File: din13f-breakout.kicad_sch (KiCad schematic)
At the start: 5 parts, among them J1 DB15_Female_HighDensity, J2 RCJ-017, J3 Conn_01x13, J4 SDD-130J

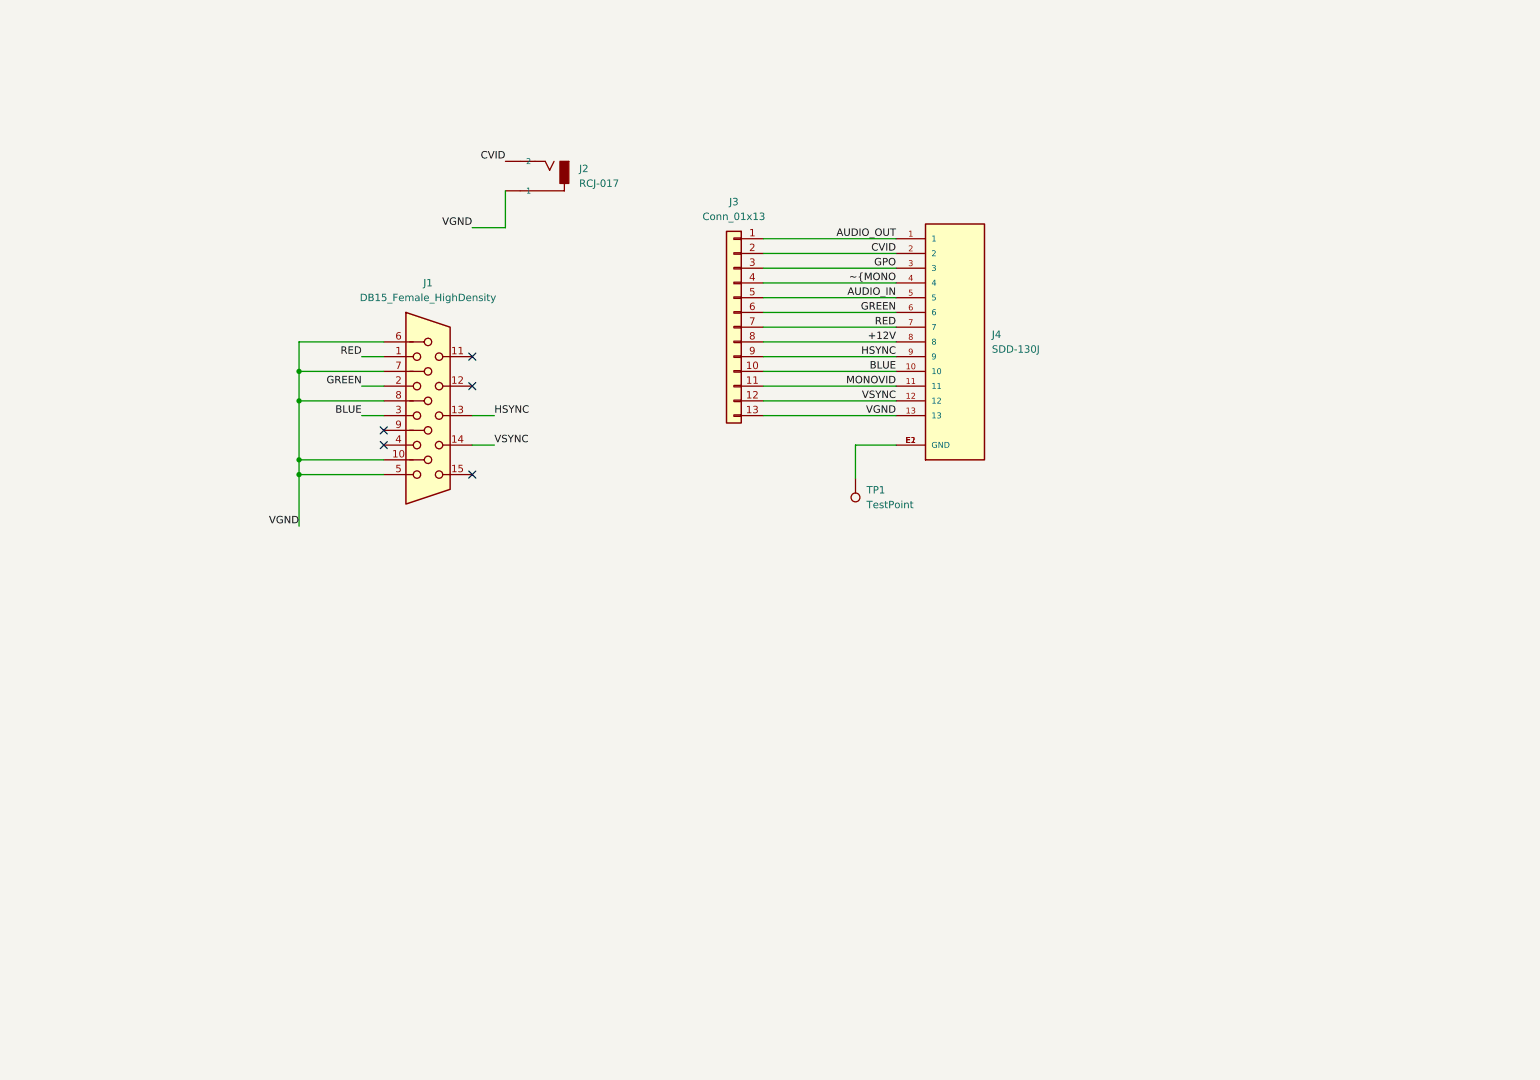
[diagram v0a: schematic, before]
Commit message: Draft of SCART version, no RGB voltage ampl yet
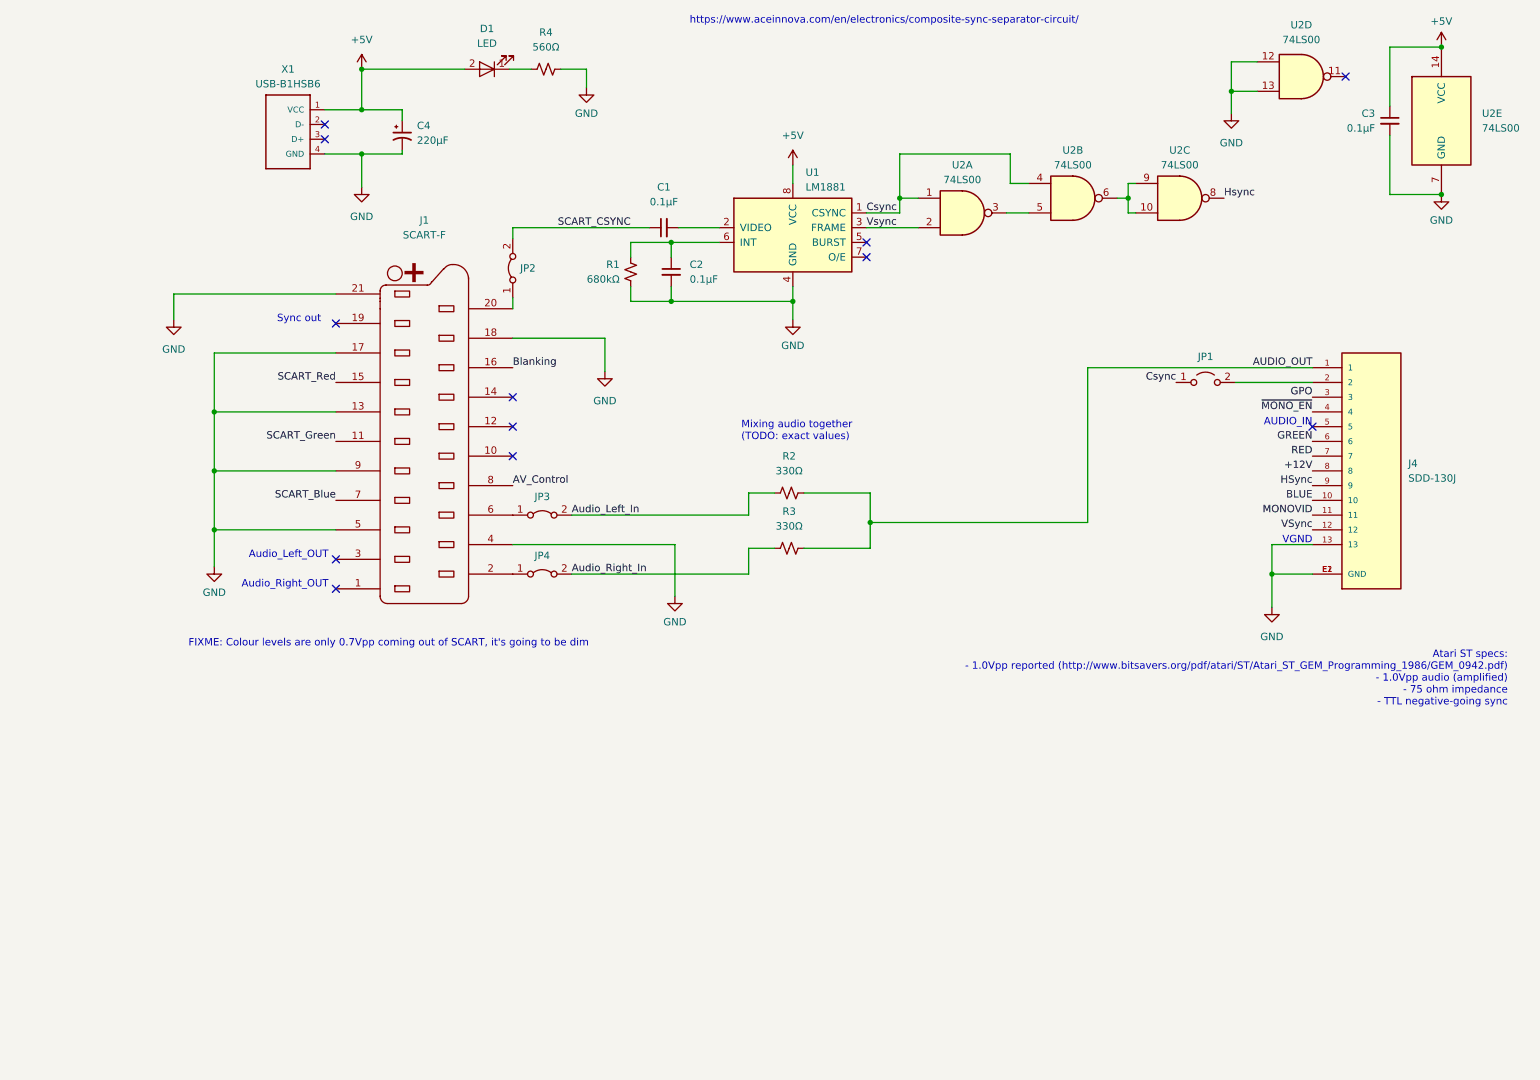
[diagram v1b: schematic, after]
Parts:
- removed J1: DB15_Female_HighDensity, Connector_TE_AMP_HD15:FIXED-1-1734530-1, symbol Connector:DB15_Female_HighDensity
- removed J2: RCJ-017, Jacks:CUI_RCJ-017, symbol RCJ-017:RCJ-017
- removed J3: Conn_01x13, Connectors:13p_GrabPads, symbol Connector_Generic:Conn_01x13
- removed TP1: TestPoint, TestPoint:TestPoint_Pad_2.5x2.5mm, symbol Connector:TestPoint
- added C1, C2, C3: 0.1µF, symbol Device:C_Small
- added C4: 220µF, symbol Device:C_Polarized_Small_US
- added D1: LED, LED_THT:LED_D3.0mm, symbol bkm-129x-scart-vga-rescue:LED
- added J1: SCART-F, ninigi-scart-ra:NINIGI-SCART-RA, symbol bkm-129x-scart-vga-rescue:SCART-F
- added JP1: Jumper_2_Open, Resistor_SMD:R_0805_2012Metric_Pad1.20x1.40mm_HandSolder, symbol Jumper:Jumper_2_Open
- added JP2, JP3, JP4: Jumper_2_Bridged, symbol Jumper:Jumper_2_Bridged
- added R1: 680kΩ, Resistor_SMD:R_0805_2012Metric_Pad1.20x1.40mm_HandSolder, symbol Device:R_Small_US
- added R2, R3: 330Ω, Resistor_SMD:R_0805_2012Metric_Pad1.20x1.40mm_HandSolder, symbol Device:R_Small_US
- added R4: 560Ω, Resistor_SMD:R_0805_2012Metric_Pad1.20x1.40mm_HandSolder, symbol Device:R_Small_US
- added U1: LM1881, Package_SO:SOIC-8_3.9x4.9mm_P1.27mm, symbol Video:LM1881
- added U2: 74LS00, Package_DIP:DIP-14_W7.62mm_Socket_LongPads, symbol 74xx:74LS00
- added X1: USB-B1HSB6, OST_USB-B1HSB6, symbol USB-B1HSB6-2:USB-B1HSB6
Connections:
- net VGND is gone; now on net GND: J4.13
- net AUDIO_OUT: now also R2.2, R3.2
- net GND: now reaches J4.E1 (GND), J4.E2 (GND)
- net GND: now also C2.2, C3.2, C4.2, J1.13 (P13), J1.17 (P17), J1.18 (P18), J1.21 (P21), J1.4 (P4), J1.5 (P5), J1.9 (P9), R1.2, R4.2, U1.4 (GND), U2.12, U2.13, U2.7 (GND), X1.4 (GND)
- net AUDIO_IN: no longer names the net of J4.5
- net CVID: no longer names the net of J4.2
- net CVID: now also JP1.2 (B)
- net HSYNC renamed HSync
- net VSYNC renamed VSync
- net ~{MONO renamed ~{MONO_EN}
- new net: J1.2 (P2), JP4.1 (A)
- new net: J1.20 (P20), JP2.1 (A)
- new net: J1.6 (P6), JP3.1 (A)
- new net: C2.1, R1.1, U1.6 (INT)
- new net: C1.2, U1.2 (VIDEO)
- new net: U2.3, U2.5
- new net: U2.10, U2.6, U2.9
- new net: D1.1 (K), R4.1
- new net +5V: C3.1, C4.1, D1.2 (A), U1.8 (VCC), U2.14 (VCC), X1.1 (VCC)
- new net AV_Control: J1.8 (P8)
- new net Audio_Left_In: JP3.2 (B), R2.1
- new net Audio_Right_In: JP4.2 (B), R3.1
- new net Blanking: J1.16 (P16)
- new net Csync: JP1.1 (A), U1.1 (CSYNC), U2.1, U2.4
- new net Hsync: U2.8
- new net SCART_Blue: J1.7 (P7)
- new net SCART_CSYNC: C1.1, JP2.2 (B)
- new net SCART_Green: J1.11 (P11)
- new net SCART_Red: J1.15 (P15)
- new net Vsync: U1.3 (FRAME), U2.2
- no-connect marks 5 -> 12
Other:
- note added: "AUDIO_IN"
- note added: "Atari ST specs: - 1.0Vpp reported (http://www.bitsavers.org/pdf/atari/ST/Atari_ST_GEM_Programming_1986/GEM_0942.pdf) - 1.0Vpp audio (amplified) - 75 ohm impedance - TTL negative-going sync"
- note added: "Audio_Left_OUT"
- note added: "Audio_Right_OUT"
- note added: "FIXME: Colour levels are only 0.7Vpp coming out of SCART, it's going to be dim"
- note added: "Mixing audio together (TODO: exact values)"
- note added: "Sync out"
- note added: "VGND"
- note added: "https://www.aceinnova.com/en/electronics/composite-sync-separator-circuit/"
- moved on the sheet: J4

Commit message: WIP for op-amps
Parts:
- added R10, R11, R12: 4.3kΩ, Resistor_SMD:R_0805_2012Metric_Pad1.20x1.40mm_HandSolder, symbol Device:R_Small_US
- added R5, R6: 1kΩ, Resistor_SMD:R_0805_2012Metric_Pad1.20x1.40mm_HandSolder, symbol Device:R_Small_US
- added R7, R8, R9: 10kΩ, Resistor_SMD:R_0805_2012Metric_Pad1.20x1.40mm_HandSolder, symbol Device:R_Small_US
- added U3: ~, Package_SO:SOIC-14_3.9x8.7mm_P1.27mm, symbol Amps:MCP6499
- C1, C2, C3: footprint (none) -> Capacitor_SMD:C_0805_2012Metric_Pad1.18x1.45mm_HandSolder
- C4: footprint (none) -> Capacitor_THT:CP_Radial_D8.0mm_P3.50mm
- J4: footprint CUI_SDD-130J -> SDD-130J:CUI_SDD-130J
- JP2, JP3, JP4: footprint (none) -> Jumper:SolderJumper-2_P1.3mm_Bridged_RoundedPad1.0x1.5mm
- X1: footprint OST_USB-B1HSB6 -> USB-B1HSB6:OST_USB-B1HSB6
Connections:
- net +5V: now also R5.1, U3.4 (Vdd)
- net BLUE: now also R12.2, U3.8 (C)
- net GND: now also R6.2, R7.1, R8.1, R9.1, U3.11 (Vss)
- net GREEN: now also R11.2, U3.7 (B)
- net RED: now also R10.2, U3.1 (A)
- net SCART_Blue: now also U3.10 (C+)
- net SCART_Green: now also U3.5 (B+)
- net SCART_Red: now also U3.3 (A+)
- new net: R5.2, R6.1, U3.12 (D+)
- new net: U3.13 (D-), U3.14 (D)
- new net: R12.1, R9.2, U3.9 (C-)
- new net: R10.1, R7.2, U3.2 (A-)
- new net: R11.1, R8.2, U3.6 (B-)
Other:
- note added: "Colour levels are only 0.7Vpp coming out of SCART, it's going to be dim so we're going to try and beef it up with this op amp"
- note added: "TODO: 4.3k seems hard to find, let's monkey with this math"
- note added: "Unused"
- note removed: "FIXME: Colour levels are only 0.7Vpp coming out of SCART, it's going to be dim"

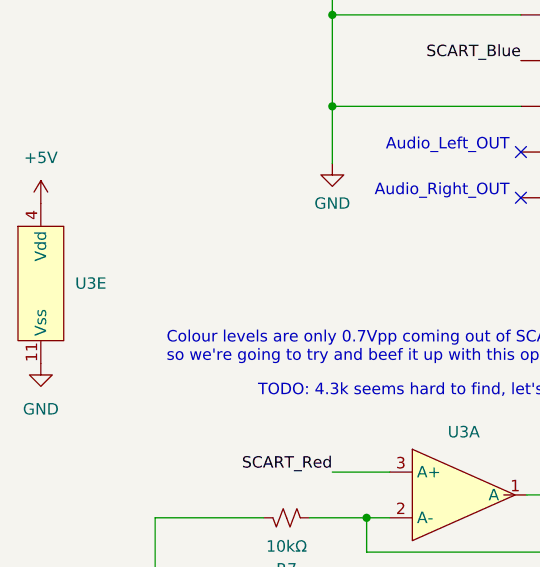
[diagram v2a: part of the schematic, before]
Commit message: Bypass cap for amp
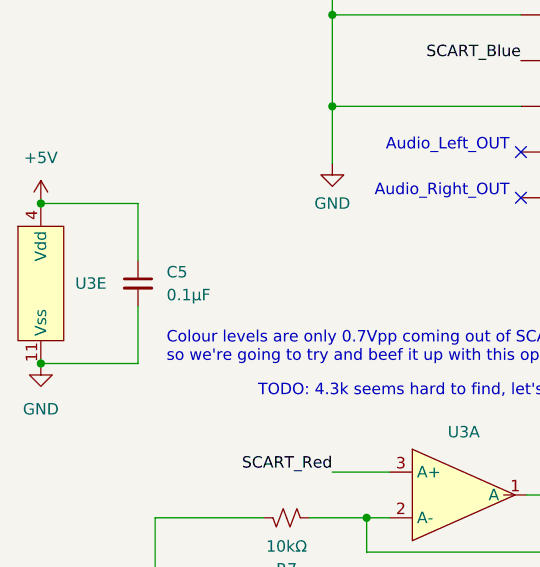
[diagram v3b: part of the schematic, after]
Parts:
- added C5: 0.1µF, Capacitor_SMD:C_0805_2012Metric_Pad1.18x1.45mm_HandSolder, symbol Device:C_Small
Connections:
- net +5V: now also C5.1
- net GND: now also C5.2
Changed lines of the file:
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@@
   (junction (at 267.97 21.59) (diameter 0) (color 0 0 0 0)
   )
+  (junction (at 24.13 133.35) (diameter 0) (color 0 0 0 0)
+  )
   (junction (at 60.325 167.64) (diameter 0) (color 0 0 0 0)
   )
   (junction (at 56.515 104.775) (diameter 0) (color 0 0 0 0)
+  )
+  (junction (at 24.13 115.57) (diameter 0) (color 0 0 0 0)
   )
   (junction (at 56.515 94.615) (diameter 0) (color 0 0 0 0)
@@
     (stroke (width 0) (type default))
   )
+  (wire (pts (xy 34.925 127) (xy 34.925 133.35))
+    (stroke (width 0) (type default))
+  )
   (wire (pts (xy 207.01 103.505) (xy 169.545 103.505))
     (stroke (width 0) (type default))
@@
     (stroke (width 0) (type default))
   )
+  (wire (pts (xy 34.925 133.35) (xy 24.13 133.35))
+    (stroke (width 0) (type default))
+  )
   (wire (pts (xy 77.47 74.295) (xy 56.515 74.295))
     (stroke (width 0) (type default))
@@
     (stroke (width 0) (type default))
   )
+  (wire (pts (xy 34.925 115.57) (xy 24.13 115.57))
+    (stroke (width 0) (type default))
+  )
   (wire (pts (xy 135.255 55.245) (xy 128.27 55.245))
     (stroke (width 0) (type default))
@@
   )
   (wire (pts (xy 107.95 64.77) (xy 107.95 66.675))
+    (stroke (width 0) (type default))
+  )
+  (wire (pts (xy 34.925 121.92) (xy 34.925 115.57))
     (stroke (width 0) (type default))
   )
@@
         )
       )
+    )
+  )
+  (symbol (lib_id "Device:C_Small") (at 34.925 124.46 0) (unit 1)
+    (in_bom yes) (on_board yes) (dnp no) (fields_autoplaced)
+    (property "Reference" "C5" (at 38.1 123.1963 0)
+      (effects (font (size 1.27 1.27)) (justify left))
+    )
+    (property "Value" "0.1µF" (at 38.1 125.7363 0)
+      (effects (font (size 1.27 1.27)) (justify left))
+    )
+    (property "Footprint" "Capacitor_SMD:C_0805_2012Metric_Pad1.18x1.45mm_HandSolder" (at 34.925 124.46 0)
+      (effects (font (size 1.27 1.27)) hide)
+    )
+    (property "Datasheet" "~" (at 34.925 124.46 0)
+      (effects (font (size 1.27 1.27)) hide)
+    )
+    (pin "1")
+    (pin "2")
+    (instances
+      (project "din13f-breakout"
+        (path "/f613f4f9-4f4a-4ef5-a528-9642b0c971e3"
+          (reference "C5") (unit 1)
+        )
+      )

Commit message: No more DIP
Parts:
- U2: footprint Package_DIP:DIP-14_W7.62mm_Socket_LongPads -> Package_SO:SOIC-14_3.9x8.7mm_P1.27mm
- U3: value ~ -> MCP6499
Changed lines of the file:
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@@
       (effects (font (size 1.27 1.27)))
     )
-    (property "Value" "~" (at 146.05 167.64 0)
-      (effects (font (size 1.27 1.27)))
+    (property "Value" "MCP6499" (at 146.05 167.64 0)
+      (effects (font (size 1.27 1.27)) hide)
     )
     (property "Footprint" "Package_SO:SOIC-14_3.9x8.7mm_P1.27mm" (at 146.05 167.64 0)
@@
       (effects (font (size 1.27 1.27)))
     )
-    (property "Value" "~" (at 70.485 184.15 0)
-      (effects (font (size 1.27 1.27)))
+    (property "Value" "MCP6499" (at 70.485 184.15 0)
+      (effects (font (size 1.27 1.27)) hide)
     )
     (property "Footprint" "Package_SO:SOIC-14_3.9x8.7mm_P1.27mm" (at 70.485 184.15 0)
@@
       (effects (font (size 1.27 1.27)))
     )
-    (property "Footprint" "Package_DIP:DIP-14_W7.62mm_Socket_LongPads" (at 204.47 47.625 0)
+    (property "Footprint" "Package_SO:SOIC-14_3.9x8.7mm_P1.27mm" (at 204.47 47.625 0)
       (effects (font (size 1.27 1.27)) hide)
     )
@@
       (effects (font (size 1.27 1.27)) (justify left))
     )
-    (property "Footprint" "Package_DIP:DIP-14_W7.62mm_Socket_LongPads" (at 267.97 34.29 0)
+    (property "Footprint" "Package_SO:SOIC-14_3.9x8.7mm_P1.27mm" (at 267.97 34.29 0)
       (effects (font (size 1.27 1.27)) hide)
     )
@@
       (effects (font (size 1.27 1.27)))
     )
-    (property "Footprint" "Package_DIP:DIP-14_W7.62mm_Socket_LongPads" (at 185.42 50.165 0)
+    (property "Footprint" "Package_SO:SOIC-14_3.9x8.7mm_P1.27mm" (at 185.42 50.165 0)
       (effects (font (size 1.27 1.27)) hide)
     )
@@
       (effects (font (size 1.27 1.27)))
     )
-    (property "Value" "~" (at 70.485 147.955 0)
-      (effects (font (size 1.27 1.27)))
+    (property "Value" "MCP6499" (at 70.485 147.955 0)
+      (effects (font (size 1.27 1.27)) hide)
     )
     (property "Footprint" "Package_SO:SOIC-14_3.9x8.7mm_P1.27mm" (at 70.485 147.955 0)
@@
       (effects (font (size 1.27 1.27)))
     )
-    (property "Footprint" "Package_DIP:DIP-14_W7.62mm_Socket_LongPads" (at 222.885 47.625 0)
+    (property "Footprint" "Package_SO:SOIC-14_3.9x8.7mm_P1.27mm" (at 222.885 47.625 0)
       (effects (font (size 1.27 1.27)) hide)
     )
@@
       (effects (font (size 1.27 1.27)))
     )
-    (property "Footprint" "Package_DIP:DIP-14_W7.62mm_Socket_LongPads" (at 243.84 26.67 0)
+    (property "Footprint" "Package_SO:SOIC-14_3.9x8.7mm_P1.27mm" (at 243.84 26.67 0)
       (effects (font (size 1.27 1.27)) hide)
     )
@@
       (effects (font (size 1.27 1.27)) (justify left))
     )
-    (property "Value" "~" (at 24.13 124.46 0)
-      (effects (font (size 1.27 1.27)))
+    (property "Value" "MCP6499" (at 24.13 124.46 0)
+      (effects (font (size 1.27 1.27)) hide)
     )
     (property "Footprint" "Package_SO:SOIC-14_3.9x8.7mm_P1.27mm" (at 24.13 124.46 0)
@@
       (effects (font (size 1.27 1.27)))
     )
-    (property "Value" "~" (at 70.485 165.1 0)
-      (effects (font (size 1.27 1.27)))
+    (property "Value" "MCP6499" (at 70.485 165.1 0)
+      (effects (font (size 1.27 1.27)) hide)
     )
     (property "Footprint" "Package_SO:SOIC-14_3.9x8.7mm_P1.27mm" (at 70.485 165.1 0)
